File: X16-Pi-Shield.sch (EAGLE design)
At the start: 39 parts, among them J3 CONN_DF13-4P-1.25DSA, J4 HTST-110-04-L-D-RA, J5 BM04B-GHS-TBT, U1 INA260AIPW, U2 AZ1117IH-3.3TRG1, U3 BNO080

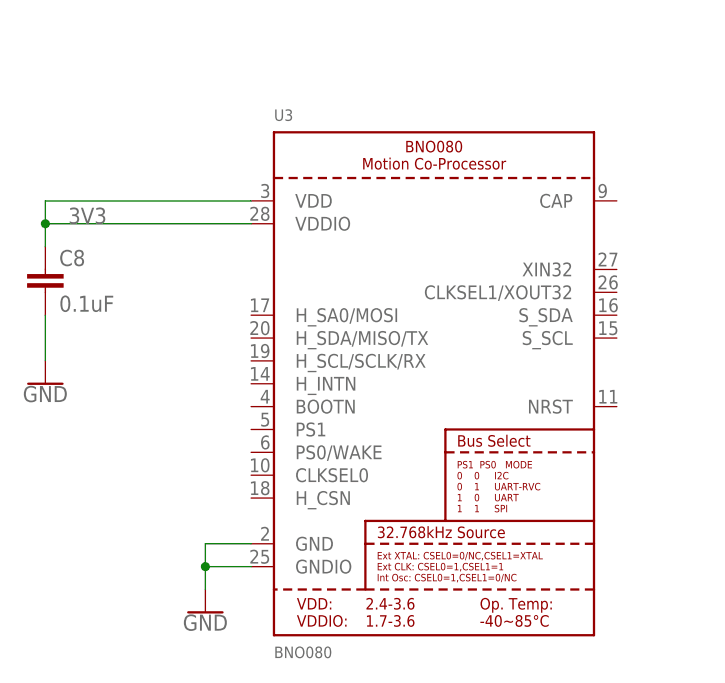
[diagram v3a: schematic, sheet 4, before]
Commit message: added new imu
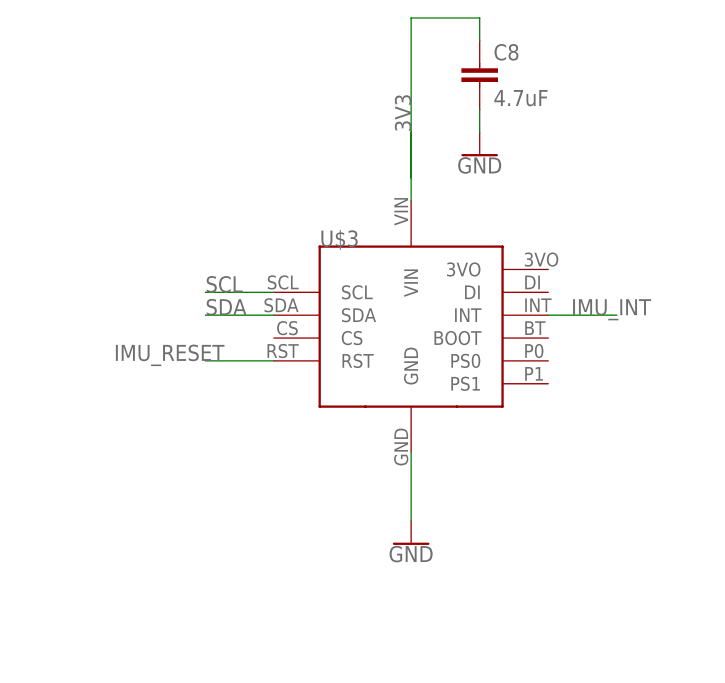
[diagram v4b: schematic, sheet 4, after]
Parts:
- removed U3: BNO080, X16-Pi-Shield:BNO080
- added U$3: ADAFRUIT-BNO080, X16-Pi-Shield:ADAFRUIT-BNO080
- C8: value 0.1uF -> 4.7uF; device SparkFun-Capacitors:0.1UF-0603-25V-(+80/-20%) -> SparkFun-Capacitors:4.7UF0603
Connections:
- removed net 3VO: U$2.3VO
- new net N$6: U$3.VIN
- net 3V3: no longer U3.VDD, U3.VDDIO
- net GND: now also U$3.GND; no longer U3.GND, U3.GNDIO
- net IMU_INT: now also U$3.INT
- net IMU_RESET: now also U$3.RST
- net SCL: now also U$3.SCL
- net SDA: now also U$3.SDA
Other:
- moved on the sheet: C8
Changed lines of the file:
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@@
 <class number="0" name="default" width="0" drill="0">
+</class>
+<class number="2" name="lowpower" width="0.254" drill="0.381">
 </class>
 </classes>
@@
 <part name="GND1" library="SparkFun-PowerSymbols" deviceset="GND" device=""/>
 <part name="FRAME4" library="SparkFun-Aesthetics" library_urn="urn:adsk.eagle:library:507" deviceset="FRAME-A4L" device=""/>
-<part name="U3" library="X16-Pi-Shield" deviceset="BNO080" device="" value="BNO080"/>
-<part name="C8" library="SparkFun-Capacitors" library_urn="urn:adsk.eagle:library:510" deviceset="0.1UF" device="-0603-25V-(+80/-20%)" package3d_urn="urn:adsk.eagle:package:41385090/1" value="0.1uF"/>
+<part name="U$3" library="X16-Pi-Shield" deviceset="ADAFRUIT-BNO080" device=""/>
+<part name="C8" library="SparkFun-Capacitors" deviceset="4.7UF" device="0603" value="4.7uF"/>
 <part name="GND15" library="SparkFun-PowerSymbols" deviceset="GND" device=""/>
 <part name="GND21" library="SparkFun-PowerSymbols" deviceset="GND" device=""/>
@@
 </segment>
 </net>
-<net name="3VO" class="0">
-<segment>
-<pinref part="U$2" gate="G$1" pin="3VO"/>
-<wire x1="76.2" y1="104.14" x2="81.28" y2="104.14" width="0.1524" layer="91"/>
-<label x="78.74" y="104.14" size="1.778" layer="95"/>
-</segment>
-</net>
 <net name="GPIO_5" class="0">
 <segment>
@@
 <attribute name="DESIGNER" x="226.26" y="6.35" size="2.54" layer="94" font="vector"/>
 </instance>
-<instance part="U3" gate="G$1" x="124.46" y="78.74" smashed="yes">
-<attribute name="NAME" x="106.68" y="107.95" size="1.27" layer="95"/>
-<attribute name="VALUE" x="106.68" y="48.26" size="1.27" layer="96"/>
-</instance>
-<instance part="C8" gate="G$1" x="81.28" y="88.9" smashed="yes">
-<attribute name="NAME" x="82.804" y="91.821" size="1.778" layer="95" font="vector"/>
-<attribute name="VALUE" x="82.804" y="86.741" size="1.778" layer="96" font="vector"/>
-</instance>
-<instance part="GND15" gate="1" x="81.28" y="78.74" smashed="yes">
-<attribute name="VALUE" x="81.28" y="78.486" size="1.778" layer="96" align="top-center"/>
-</instance>
-<instance part="GND21" gate="1" x="99.06" y="53.34" smashed="yes">
-<attribute name="VALUE" x="99.06" y="53.086" size="1.778" layer="96" align="top-center"/>
+<instance part="U$3" gate="G$1" x="121.92" y="86.36" smashed="yes">
+<attribute name="NAME" x="111.76" y="93.98" size="1.778" layer="95"/>
+</instance>
+<instance part="C8" gate="G$1" x="129.54" y="111.76" smashed="yes">
+<attribute name="NAME" x="131.064" y="114.681" size="1.778" layer="95" font="vector"/>
+<attribute name="VALUE" x="131.064" y="109.601" size="1.778" layer="96" font="vector"/>
+</instance>
+<instance part="GND15" gate="1" x="129.54" y="104.14" smashed="yes">
+<attribute name="VALUE" x="129.54" y="103.886" size="1.778" layer="96" align="top-center"/>
+</instance>
+<instance part="GND21" gate="1" x="121.92" y="60.96" smashed="yes">
+<attribute name="VALUE" x="121.92" y="60.706" size="1.778" layer="96" align="top-center"/>
 </instance>
 </instances>
@@
 </busses>
 <nets>
+<net name="SCL" class="0">
+<segment>
+<pinref part="U$3" gate="G$1" pin="SCL"/>
+<wire x1="106.68" y1="88.9" x2="99.06" y2="88.9" width="0.1524" layer="91"/>
+<label x="99.06" y="88.9" size="1.778" layer="95"/>
+</segment>
+</net>
+<net name="SDA" class="0">
+<segment>
+<pinref part="U$3" gate="G$1" pin="SDA"/>
+<wire x1="106.68" y1="86.36" x2="99.06" y2="86.36" width="0.1524" layer="91"/>
+<label x="99.06" y="86.36" size="1.778" layer="95"/>
+</segment>
+</net>
+<net name="IMU_RESET" class="0">
+<segment>
+<pinref part="U$3" gate="G$1" pin="RST"/>
+<wire x1="106.68" y1="81.28" x2="99.06" y2="81.28" width="0.1524" layer="91"/>
+<label x="88.9" y="81.28" size="1.778" layer="95"/>
+</segment>
+</net>
+<net name="N$6" class="0">
+<segment>
+<pinref part="U$3" gate="G$1" pin="VIN"/>
+<wire x1="121.92" y1="99.06" x2="121.92" y2="106.68" width="0.1524" layer="91"/>
+</segment>
+</net>
+<net name="IMU_INT" class="0">
+<segment>
+<pinref part="U$3" gate="G$1" pin="INT"/>
+<wire x1="137.16" y1="86.36" x2="144.78" y2="86.36" width="0.1524" layer="91"/>
+<label x="139.7" y="86.36" size="1.778" layer="95"/>
+</segment>
+</net>
+<net name="GND" class="0">
+<segment>
+<pinref part="C8" gate="G$1" pin="2"/>
+<wire x1="129.54" y1="109.22" x2="129.54" y2="106.68" width="0.1524" layer="91"/>
+<pinref part="GND15" gate="1" pin="GND"/>
+</segment>
+<segment>
+<pinref part="U$3" gate="G$1" pin="GND"/>
+<wire x1="121.92" y1="71.12" x2="121.92" y2="63.5" width="0.1524" layer="91"/>
+<pinref part="GND21" gate="1" pin="GND"/>
+</segment>
+</net>
 <net name="3V3" class="0">
 <segment>
-<pinref part="U3" gate="G$1" pin="VDDIO"/>
-<wire x1="104.14" y1="96.52" x2="81.28" y2="96.52" width="0.1524" layer="91"/>
+<wire x1="121.92" y1="101.6" x2="121.92" y2="119.38" width="0.1524" layer="91"/>
+<label x="121.92" y="106.68" size="1.778" layer="95" rot="R90"/>
+<wire x1="121.92" y1="119.38" x2="129.54" y2="119.38" width="0.1524" layer="91"/>
+<wire x1="129.54" y1="119.38" x2="129.54" y2="116.84" width="0.1524" layer="91"/>
 <pinref part="C8" gate="G$1" pin="1"/>
-<wire x1="81.28" y1="96.52" x2="81.28" y2="93.98" width="0.1524" layer="91"/>
-<label x="83.82" y="96.52" size="1.778" layer="95"/>
-<pinref part="U3" gate="G$1" pin="VDD"/>
-<wire x1="104.14" y1="99.06" x2="81.28" y2="99.06" width="0.1524" layer="91"/>
-<wire x1="81.28" y1="99.06" x2="81.28" y2="96.52" width="0.1524" layer="91"/>
-<junction x="81.28" y="96.52"/>
-</segment>
-</net>
-<net name="GND" class="0">
-<segment>
-<pinref part="C8" gate="G$1" pin="2"/>
-<wire x1="81.28" y1="86.36" x2="81.28" y2="81.28" width="0.1524" layer="91"/>
-<pinref part="GND15" gate="1" pin="GND"/>
-</segment>
-<segment>
-<pinref part="U3" gate="G$1" pin="GNDIO"/>
-<wire x1="104.14" y1="58.42" x2="99.06" y2="58.42" width="0.1524" layer="91"/>
-<pinref part="GND21" gate="1" pin="GND"/>
-<wire x1="99.06" y1="58.42" x2="99.06" y2="55.88" width="0.1524" layer="91"/>
-<pinref part="U3" gate="G$1" pin="GND"/>
-<wire x1="104.14" y1="60.96" x2="99.06" y2="60.96" width="0.1524" layer="91"/>
-<wire x1="99.06" y1="60.96" x2="99.06" y2="58.42" width="0.1524" layer="91"/>
-<junction x="99.06" y="58.42"/>
-</segment>
-</net>
+</segment>
+</net>

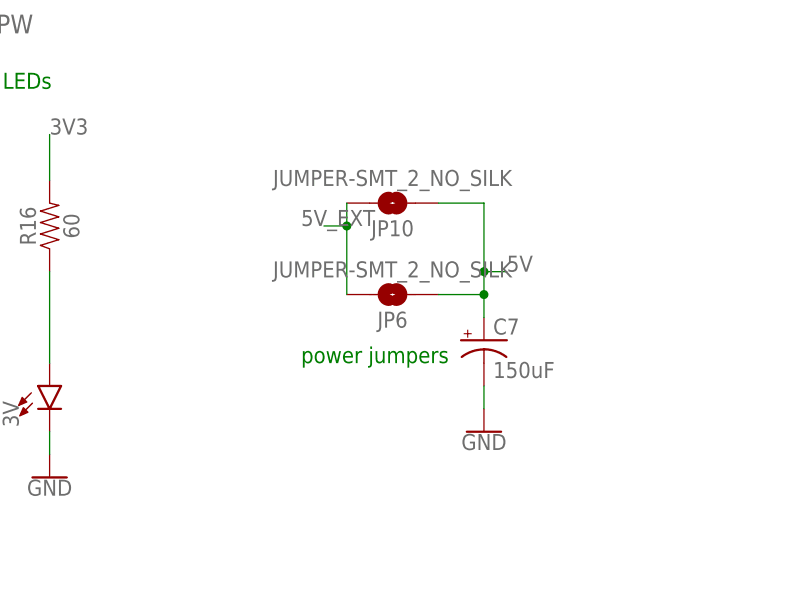
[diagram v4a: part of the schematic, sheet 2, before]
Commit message: added new imu
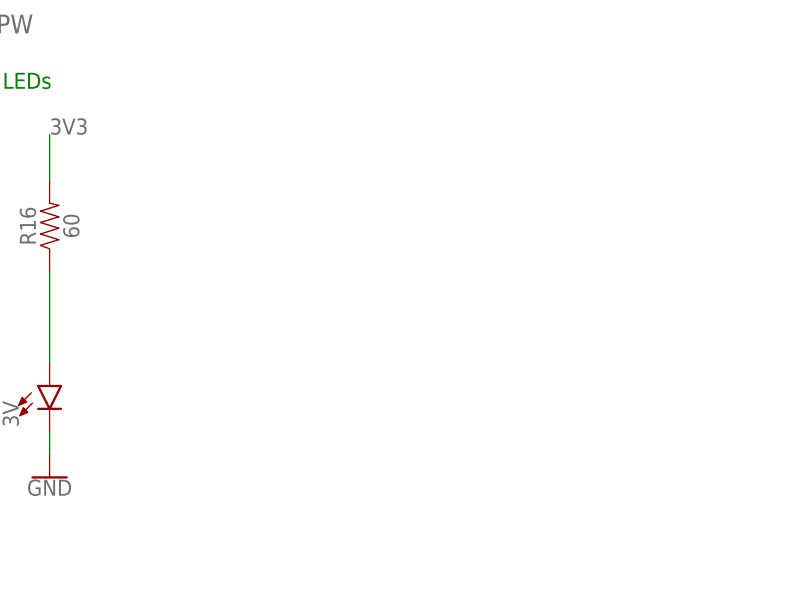
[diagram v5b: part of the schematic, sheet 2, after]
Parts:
- removed C7: 150uF, X15-Pi-Shield-Parts:C-TANTALUM(10UF_150UF)
- removed JP10, JP6: JUMPER-SMT_2_NO_SILK, SparkFun-Jumpers:JUMPER-SMT_2_NO_SILK
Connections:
- net 5V: no longer C7.+, JP10.1, JP6.1
- net 5V_EXT: no longer JP10.2, JP6.2
- net GND: no longer C7.-
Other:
- note removed: "power jumpers"
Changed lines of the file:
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@@
 <part name="TP7" library="SparkFun-Connectors" deviceset="TEST-POINT" device="3"/>
 <part name="TP8" library="SparkFun-Connectors" deviceset="TEST-POINT" device="3"/>
-<part name="GND11" library="SparkFun-PowerSymbols" deviceset="GND" device=""/>
-<part name="C7" library="X15-Pi-Shield-Parts" deviceset="C-TANTALUM(10UF_150UF)" device="" value="150uF"/>
-<part name="JP6" library="SparkFun-Jumpers" deviceset="JUMPER-SMT_2_NO" device="_SILK"/>
-<part name="JP10" library="SparkFun-Jumpers" deviceset="JUMPER-SMT_2_NO" device="_SILK"/>
 <part name="C1" library="SparkFun-Capacitors" library_urn="urn:adsk.eagle:library:510" deviceset="10UF-POLAR" device="-0603-6.3V-20%(TANT)" package3d_urn="urn:adsk.eagle:package:41385074/1" value="120uF"/>
 <part name="C2" library="SparkFun-Capacitors" library_urn="urn:adsk.eagle:library:510" deviceset="10UF-POLAR" device="-0603-6.3V-20%(TANT)" package3d_urn="urn:adsk.eagle:package:41385074/1" value="120uF"/>
@@
 <text x="27.94" y="152.4" size="1.778" layer="91">5v test point</text>
 <text x="25.4" y="144.78" size="1.778" layer="91">GND test point</text>
-<text x="200.66" y="73.66" size="1.778" layer="91">power jumpers</text>
 </plain>
 <instances>
@@
 <attribute name="NAME" x="48.26" y="147.32" size="1.778" layer="95" font="vector"/>
 <attribute name="VALUE" x="48.26" y="142.24" size="1.778" layer="96" font="vector"/>
-</instance>
-<instance part="GND11" gate="1" x="220.98" y="66.04" smashed="yes">
-<attribute name="VALUE" x="220.98" y="65.786" size="1.778" layer="96" align="top-center"/>
-</instance>
-<instance part="C7" gate="G$1" x="220.98" y="76.2" smashed="yes">
-<attribute name="NAME" x="221.996" y="76.835" size="1.778" layer="95"/>
-<attribute name="VALUE" x="221.996" y="72.009" size="1.778" layer="96"/>
-</instance>
-<instance part="JP6" gate="G$1" x="210.82" y="81.28" smashed="yes" rot="R180">
-<attribute name="NAME" x="210.82" y="78.486" size="1.778" layer="95" font="vector" rot="R180" align="center"/>
-<attribute name="VALUE" x="210.82" y="84.074" size="1.778" layer="96" font="vector" rot="R180" align="center"/>
-</instance>
-<instance part="JP10" gate="G$1" x="210.82" y="91.44" smashed="yes" rot="R180">
-<attribute name="NAME" x="210.82" y="88.646" size="1.778" layer="95" font="vector" rot="R180" align="center"/>
-<attribute name="VALUE" x="210.82" y="94.234" size="1.778" layer="96" font="vector" rot="R180" align="center"/>
 </instance>
 </instances>
@@
 <wire x1="50.8" y1="152.4" x2="40.64" y2="152.4" width="0.1524" layer="91"/>
 </segment>
-<segment>
-<wire x1="215.9" y1="81.28" x2="220.98" y2="81.28" width="0.1524" layer="91"/>
-<wire x1="220.98" y1="81.28" x2="220.98" y2="78.74" width="0.1524" layer="91"/>
-<wire x1="215.9" y1="91.44" x2="220.98" y2="91.44" width="0.1524" layer="91"/>
-<wire x1="220.98" y1="91.44" x2="220.98" y2="83.82" width="0.1524" layer="91"/>
-<junction x="220.98" y="81.28"/>
-<wire x1="220.98" y1="83.82" x2="220.98" y2="81.28" width="0.1524" layer="91"/>
-<wire x1="220.98" y1="83.82" x2="223.52" y2="83.82" width="0.1524" layer="91"/>
-<junction x="220.98" y="83.82"/>
-<label x="223.52" y="83.82" size="1.778" layer="95"/>
-<pinref part="C7" gate="G$1" pin="+"/>
-<pinref part="JP6" gate="G$1" pin="1"/>
-<pinref part="JP10" gate="G$1" pin="1"/>
-</segment>
 </net>
 <net name="N$7" class="0">
@@
 <label x="48.26" y="144.78" size="1.778" layer="95"/>
 <wire x1="50.8" y1="144.78" x2="40.64" y2="144.78" width="0.1524" layer="91"/>
-</segment>
-<segment>
-<wire x1="220.98" y1="71.12" x2="220.98" y2="68.58" width="0.1524" layer="91"/>
-<pinref part="GND11" gate="1" pin="GND"/>
-<pinref part="C7" gate="G$1" pin="-"/>
 </segment>
 </net>
@@
 <label x="86.36" y="162.56" size="1.778" layer="95"/>
 </segment>
-<segment>
-<pinref part="JP10" gate="G$1" pin="2"/>
-<wire x1="205.74" y1="91.44" x2="205.74" y2="88.9" width="0.1524" layer="91"/>
-<wire x1="205.74" y1="88.9" x2="203.2" y2="88.9" width="0.1524" layer="91"/>
-<pinref part="JP6" gate="G$1" pin="2"/>
-<wire x1="205.74" y1="81.28" x2="205.74" y2="88.9" width="0.1524" layer="91"/>
-<junction x="205.74" y="88.9"/>
-<label x="200.66" y="88.9" size="1.778" layer="95"/>
-</segment>
-</net>
+</net>

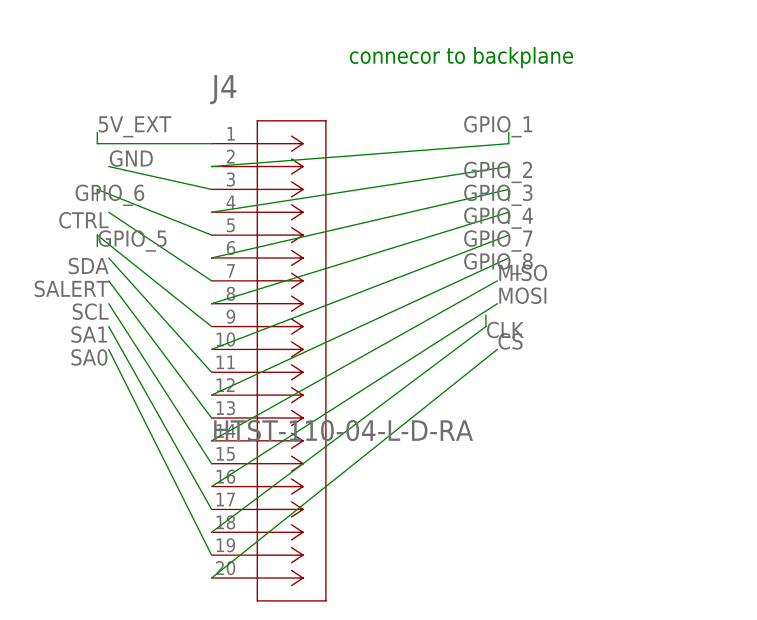
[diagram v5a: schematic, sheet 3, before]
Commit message: updated connector footprint and connector connections
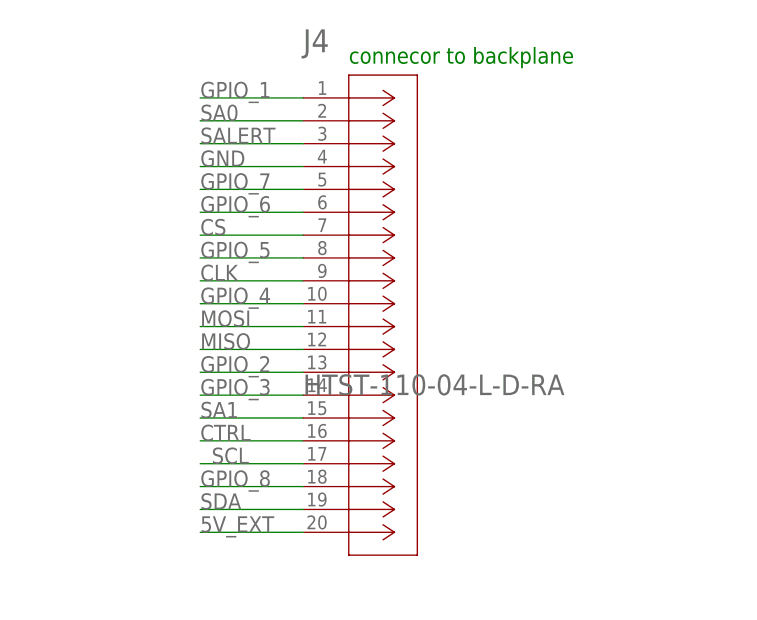
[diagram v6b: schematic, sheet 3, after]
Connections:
- removed net N$6: U$3.VIN
- net 3V3: now also U$3.VIN
- net 5V_EXT: now also J4.20; no longer J4.1
- net CLK: now also J4.9; no longer J4.18
- net CS: now also J4.7; no longer J4.20
- net CTRL: now also J4.16; no longer J4.7
- net GND: now also J4.4; no longer J4.3
- net GPIO_1: now also J4.1; no longer J4.2
- net GPIO_2: now also J4.13; no longer J4.4
- net GPIO_3: now also J4.14; no longer J4.6
- net GPIO_4: now also J4.10; no longer J4.8
- net GPIO_5: now also J4.8; no longer J4.9
- net GPIO_6: now also J4.6; no longer J4.5
- net GPIO_7: now also J4.5; no longer J4.10
- net GPIO_8: now also J4.18; no longer J4.12
- net MISO: now also J4.12; no longer J4.14
- net MOSI: now also J4.11; no longer J4.16
- net SA0: now also J4.2; no longer J4.19
- net SA1: now also J4.15; no longer J4.17
- net SALERT: now also J4.3; no longer J4.13
- net SCL: now also J4.17; no longer J4.15, U$1.GPIO12
- net SDA: now also J4.19; no longer J4.11
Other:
- moved on the sheet: J4

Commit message: remade board
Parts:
- removed TP4, TP5, TP6, TP7, TP8: TEST-POINT3, SparkFun-Connectors:TEST-POINT3
- added J1: CONN_DF13-4P-1.25DSA, X16-Pi-Shield:CONN_DF13-4P-1.25DSA
- added J2: (no value), SparkFun-Connectors:CONN_02
- added J6: BM04B-GHS-TBT, X16-Pi-Shield:BM04B-GHS-TBT
- added U$4, U$5, U$6: TESTPOINT_5.04MM, X16-ExtraComponents:TESTPOINT_5.04MM
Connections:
- new net IMU_INT_2: U$1.GPIO19, U$3.INT
- new net IMU_RESET_2: U$1.GPIO26, U$3.RST
- new net N$1: JP5.1, U1.A1
- net 3V3: now also J1.1, J6.2, U$4.TP; no longer TP6.1
- net 5V: now also U$5.TP; no longer TP7.1
- net 5V_EXT: now also J2.2
- net CLK: now also J12.5; no longer J12.2
- net CS: now also J12.4; no longer J12.5
- net GND: now also J1.4, J2.1, J6.1, U$6.TP; no longer TP8.1
- net IMU_INT: no longer U$3.INT
- net IMU_RESET: no longer U$3.RST
- net MISO: now also J12.3; no longer J12.4
- net MOSI: now also J12.2; no longer J12.3
- net SA0: no longer TP4.1
- net SA1: no longer JP5.1, TP5.1, U1.A1
- net SCL: now also J1.2, J6.3
- net SDA: now also J1.3, J6.4
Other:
- note added: "depth sensor connectors"
- note removed: "SA0 test point"
- note removed: "SA1 test point"
- moved on the sheet: J5

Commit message: finished board
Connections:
- net SCL: now also J11.3; no longer J11.2
- net SDA: now also J11.2; no longer J11.3
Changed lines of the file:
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@@
-</segment>
-<segment>
-<pinref part="J11" gate="G$1" pin="3"/>
-<wire x1="25.4" y1="55.88" x2="38.1" y2="55.88" width="0.1524" layer="91"/>
-<label x="35.56" y="55.88" size="1.778" layer="95"/>
 </segment>
 <segment>
@@
 <wire x1="142.24" y1="43.18" x2="137.16" y2="43.18" width="0.1524" layer="91"/>
 <label x="137.16" y="43.18" size="1.778" layer="95"/>
+</segment>
+<segment>
+<pinref part="J11" gate="G$1" pin="2"/>
+<wire x1="25.4" y1="53.34" x2="38.1" y2="53.34" width="0.1524" layer="91"/>
+<label x="33.02" y="53.34" size="1.778" layer="95"/>
 </segment>
 </net>
@@
 </segment>
 <segment>
-<pinref part="J11" gate="G$1" pin="2"/>
-<wire x1="25.4" y1="53.34" x2="38.1" y2="53.34" width="0.1524" layer="91"/>
-<label x="35.56" y="53.34" size="1.778" layer="95"/>
-</segment>
-<segment>
 <pinref part="U$2" gate="G$1" pin="SCL"/>
 <wire x1="45.72" y1="101.6" x2="40.64" y2="101.6" width="0.1524" layer="91"/>
@@
 <label x="137.16" y="45.72" size="1.778" layer="95"/>
 </segment>
+<segment>
+<pinref part="J11" gate="G$1" pin="3"/>
+<wire x1="25.4" y1="55.88" x2="38.1" y2="55.88" width="0.1524" layer="91"/>
+<label x="35.56" y="55.88" size="1.778" layer="95"/>
+</segment>
 </net>
